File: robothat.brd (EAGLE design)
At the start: 57.6 x 48.2 mm, 84 parts, among them IC3 78L05SMD, T1 BC847, U1 LM293AD, U2 TSM2312CX, U3 ADUM7441ARQZ, U5 TSM2312CX, U8 LM293AD

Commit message: finished first place
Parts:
- removed C3: 100n, rcl:C0805
- moved C11 128.8 mm to (35.1, 18.3), flipped to the bottom, turned to 270 degrees
- moved C7 109.7 mm to (25.4, 17.0), flipped to the bottom, turned to 180 degrees
- moved R11 106.2 mm to (30.5, 13.7), flipped to the bottom, turned to 270 degrees
- moved R9 101.0 mm to (32.8, 18.3), flipped to the bottom, turned to 90 degrees
- moved R12 90.5 mm to (29.5, 17.0), flipped to the bottom, turned to 180 degrees
- moved R15 89.5 mm to (18.0, 7.62), flipped to the bottom, turned to 90 degrees
- moved R14 89.1 mm to (19.1, 2.29), flipped to the bottom, turned to 90 degrees
- moved R4 87.4 mm to (11.7, 13.7), flipped to the bottom, turned to 270 degrees
- moved C1 86.5 mm to (9.14, 4.83), flipped to the bottom, turned to 90 degrees
- moved R1 86.4 mm to (7.11, 4.83), flipped to the bottom, turned to 90 degrees
- moved R3 85.7 mm to (13.7, 13.7), flipped to the bottom, turned to 270 degrees
- moved R2 85.6 mm to (8.13, 8.13), flipped to the bottom
- moved R10 84.6 mm to (32.8, 22.4), flipped to the bottom, turned to 90 degrees
- moved C2 84.2 mm to (9.65, 13.7), flipped to the bottom, turned to 270 degrees
- moved R13 79.2 mm to (27.7, 13.7), flipped to the bottom, turned to 90 degrees
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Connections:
- net AGND: no longer C3.1
- net AX12_RX: now also AXFUSE1.2
- net AX12_RX_P: no longer AXFUSE1.2
- net VCC: no longer C3.2
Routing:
- net BUTTON3: track 0.00 -> 12.7 mm
- net BUTTON1: track 0.00 -> 12.7 mm
- net SENSOR1: track 0.00 -> 11.4 mm, vias 0 -> 1
- net START: track 0.00 -> 10.7 mm
- net BUTTON2: track 0.00 -> 10.7 mm
- net N$18: track 0.00 -> 9.73 mm
- net N$31: track 0.00 -> 8.51 mm
- net LED3: track 0.00 -> 6.11 mm
- net LED1: track 0.00 -> 5.67 mm
- net N$33: track 0.00 -> 3.75 mm
- net N$12: track 0.00 -> 3.66 mm
- net N$41: track 0.00 -> 3.18 mm
- net N$40: track 0.00 -> 3.18 mm
- net N$39: track 0.00 -> 3.18 mm
- net SENSOR2: track 0.00 -> 3.13 mm, vias 0 -> 1
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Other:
- board size 57.6 x 48.2 mm -> 57.6 x 47.9 mm

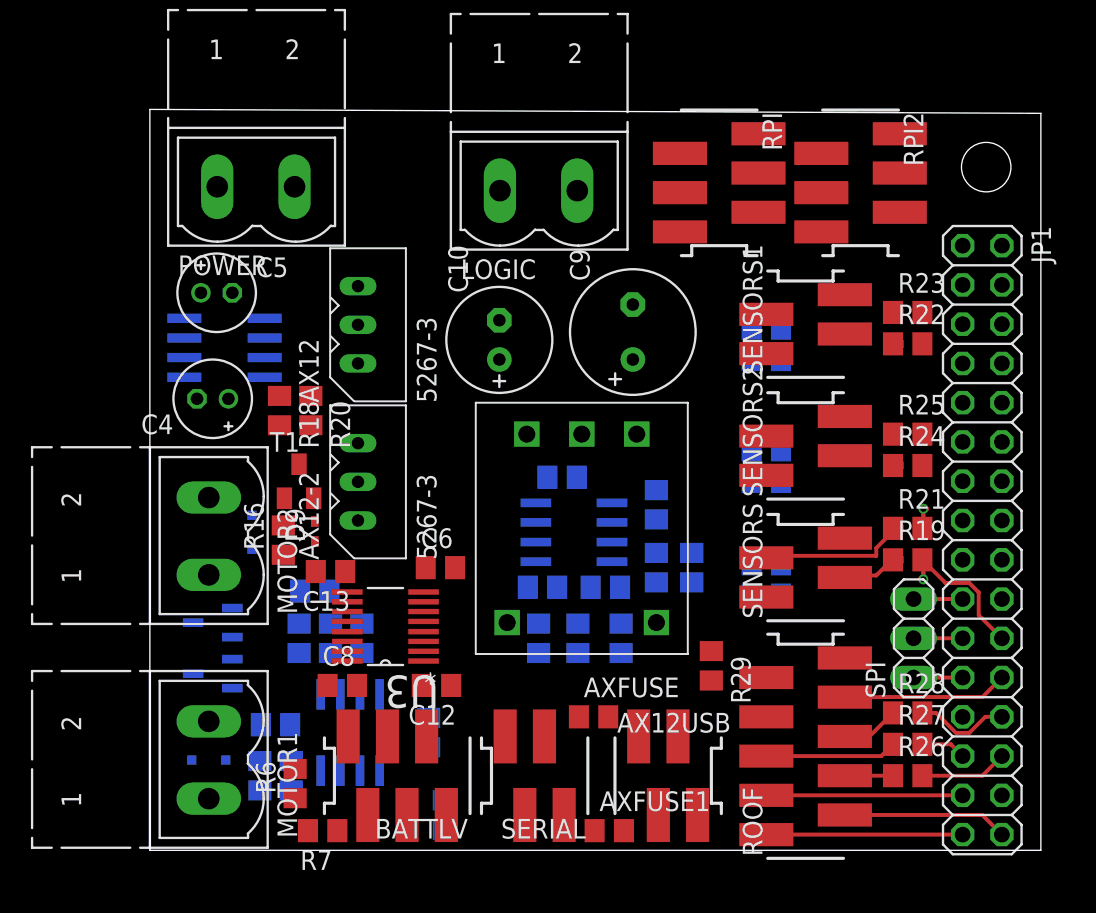
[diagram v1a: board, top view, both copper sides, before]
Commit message: routing and silkscreen done
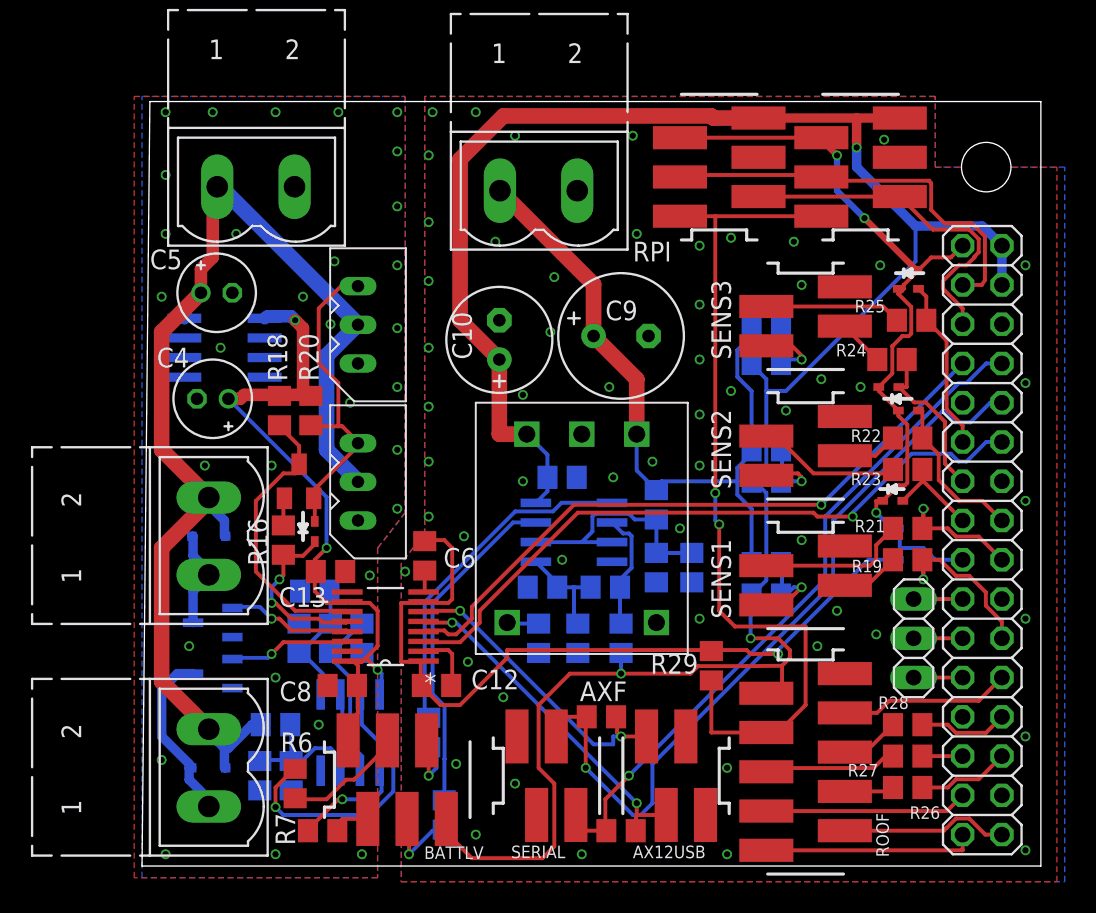
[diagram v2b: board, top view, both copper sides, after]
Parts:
- removed AXFUSE: 0R, resistor:R0805
- removed SENSORS, SENSORS1: (no value), con-amp:SMDTOP4
- added AXF: 0R, resistor:R0805
- added SENS1, SENS3: (no value), con-amp:SMDTOP4
- moved D3 12.2 mm to (48.0, 22.6), flipped to the top, turned to 0 degrees
- moved R23 10.2 mm to (49.0, 24.6)
- moved D5 9.40 mm to (49.0, 36.3), flipped to the top, turned to 0 degrees
- moved R25 7.37 mm to (49.3, 34.3)
- moved R24 6.93 mm to (48.0, 31.8)
- moved R22 6.10 mm to (49.0, 26.7)
- moved D6 5.24 mm to (47.8, 30.0), flipped to the top, turned to 0 degrees
- moved D4 4.32 mm to (49.0, 28.4), flipped to the top, turned to 0 degrees
- moved D8 2.81 mm to (3.81, 20.3), turned to 0 degrees
- moved C6 1.27 mm to (17.8, 19.1), turned to 90 degrees
- moved ROOF 1.02 mm to (42.4, 5.71)
- moved RPI 1.02 mm to (36.8, 44.2)
- moved RPI2 1.02 mm to (46.0, 44.2)
- moved C9 0.80 mm to (30.5, 33.3), turned to 0 degrees
- moved AXFUSE1 0.76 mm to (30.5, 1.27)
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- renumbered SENSORS2 to SENS2
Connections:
- net AX12_TX: now also AXF.2; no longer AXFUSE.2
- net GND: now also SENS1.4, SENS3.4; no longer SENSORS.4, SENSORS1.4
- net N$10: now also SENS2.1; no longer SENSORS1.1
- net N$11: now also SENS2.2; no longer SENSORS1.2
- net N$12: now also SENS1.2; no longer SENSORS.2
- net N$18: now also SENS1.3; no longer SENSORS.3
- net N$22: now also SENS2.3; no longer SENSORS1.3
- net N$26: now also SENS3.1; no longer SENS2.1
- net N$27: now also SENS3.2; no longer SENS2.2
- net N$28: now also SENS3.3; no longer SENS2.3
- net N$9: now also SENS1.1; no longer SENSORS.1
- net RPI_RX: now also AXF.1; no longer AXFUSE.1
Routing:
- net +5V: track 0.00 -> 151.8 mm, vias 0 -> 3
- net +3V3: track 0.00 -> 104.4 mm, vias 0 -> 4
- net VDD: track 0.00 -> 76.1 mm
- net N_RESET: track 0.00 -> 56.1 mm, vias 0 -> 2
- net RPI_RX: track 0.00 -> 50.3 mm, vias 0 -> 1
- net VCC: track 0.00 -> 49.5 mm, vias 0 -> 3
- net +12V: track 0.00 -> 45.9 mm
- net RPI_TX: track 0.00 -> 44.5 mm, vias 0 -> 1
- net MOTOR1: track 0.00 -> 44.0 mm, vias 0 -> 1
- net MOTOR2: track 0.00 -> 42.7 mm, vias 0 -> 1
- net I2C_SDA: track 0.00 -> 27.1 mm
- net I2C_SCL: track 0.00 -> 23.1 mm
- net N$14: track 0.00 -> 22.4 mm
- net AX12_RX: track 0.00 -> 22.4 mm, vias 0 -> 2
- net N$16: track 0.00 -> 21.9 mm
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- added copper zone on layer 1, net AGND
- added copper zone on layer 16, net AGND
- added copper zone on layer 1, net GND
- added copper zone on layer 16, net GND
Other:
- board size 57.6 x 47.9 mm -> 58.1 x 49.5 mm

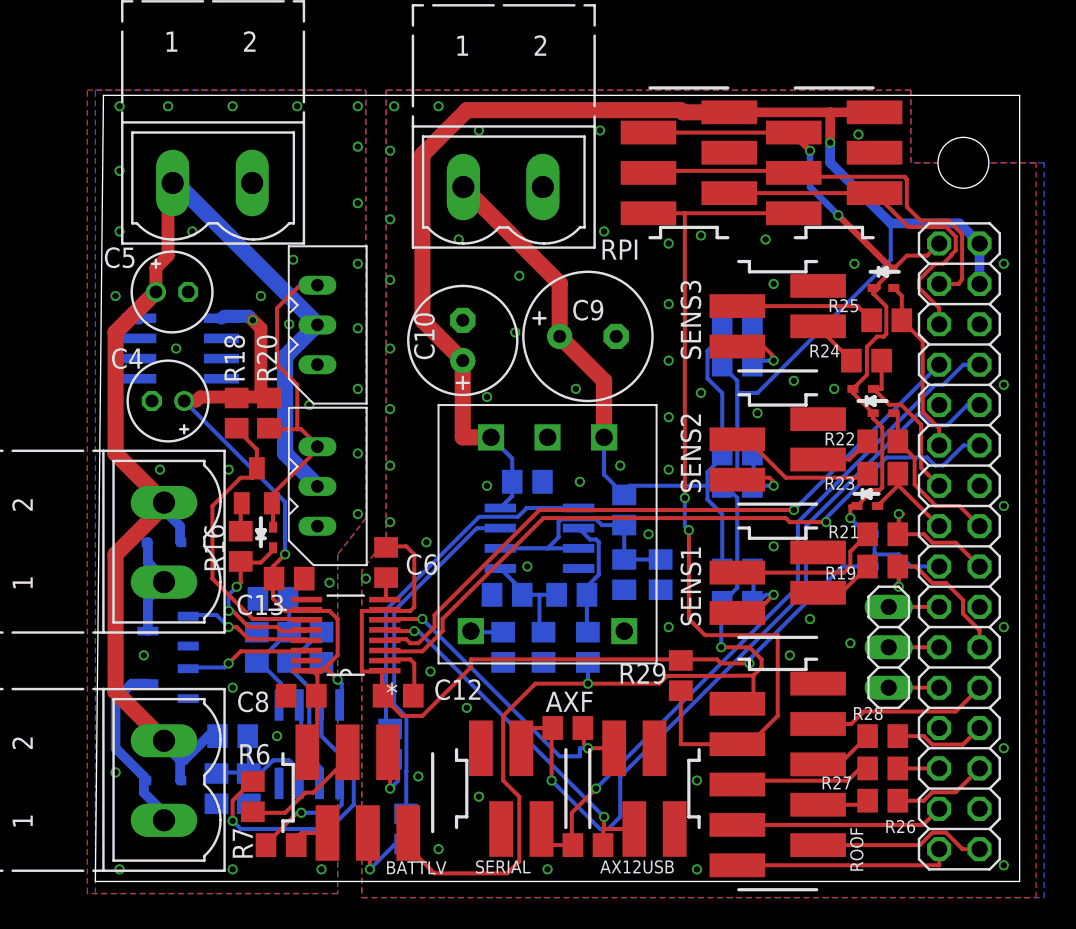
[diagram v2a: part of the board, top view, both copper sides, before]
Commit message: added schematic and pcb in pdf, added BOM
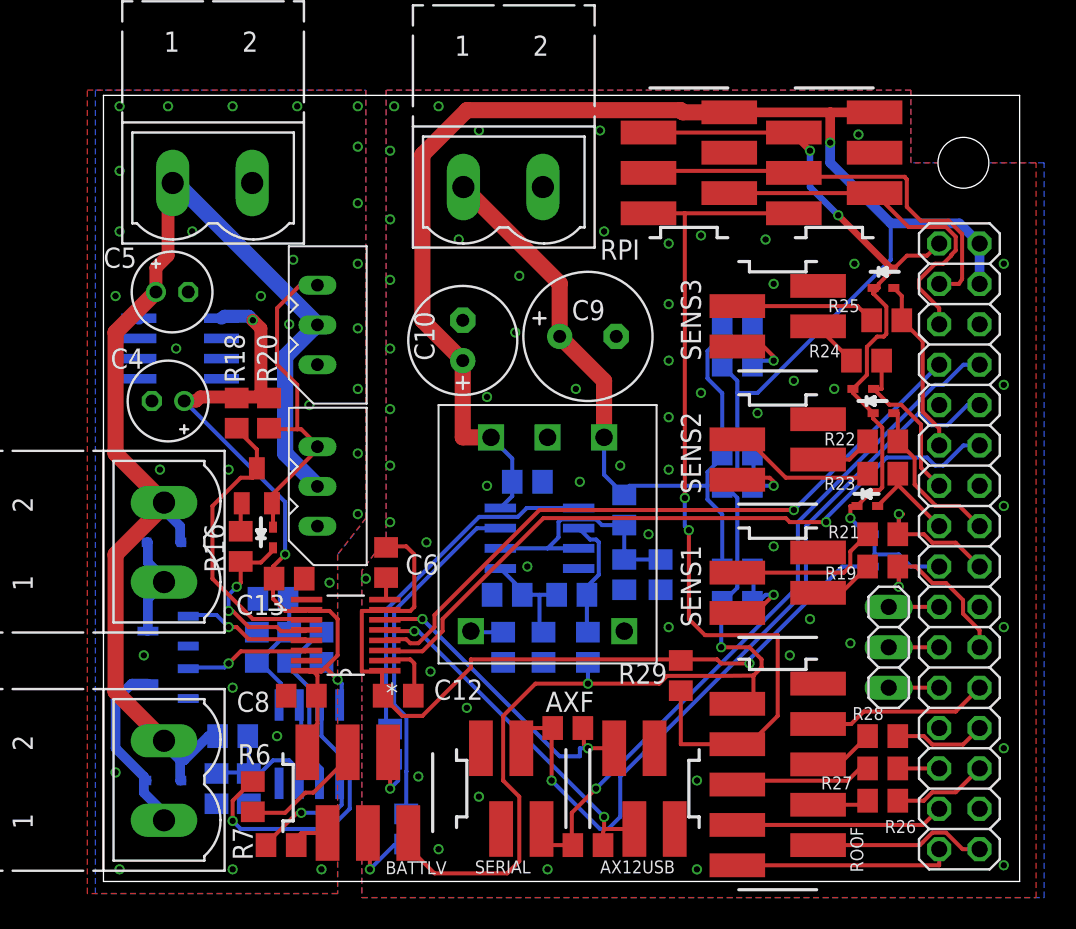
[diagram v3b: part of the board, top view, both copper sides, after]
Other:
- board size 58.1 x 49.5 mm -> 57.6 x 49.5 mm
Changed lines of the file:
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@@
 <board>
 <plain>
-<wire x1="-0.508" y1="-1.016" x2="57.638" y2="-1.016" width="0" layer="20"/>
+<wire x1="0" y1="-1.016" x2="57.638" y2="-1.016" width="0" layer="20"/>
 <wire x1="57.638" y1="-1.016" x2="57.638" y2="48.438" width="0" layer="20"/>
 <wire x1="57.638" y1="48.438" x2="0" y2="48.438" width="0" layer="20"/>
-<wire x1="0" y1="48.438" x2="-0.508" y2="-1.016" width="0" layer="20"/>
+<wire x1="0" y1="48.438" x2="0" y2="-1.016" width="0" layer="20"/>
 <hole x="54.102" y="44.196" drill="3.2"/>
 <circle x="54.102" y="44.196" radius="2.0945375" width="2.54" layer="41"/>
@@
 <wire x1="8.636" y1="2.286" x2="8.128" y2="2.794" width="0.254" layer="16"/>
 <wire x1="14.224" y1="2.286" x2="8.636" y2="2.286" width="0.254" layer="16"/>
-<wire x1="15.748" y1="3.81" x2="14.224" y2="2.286" width="0.254" layer="16"/>
-<wire x1="15.748" y1="6.096" x2="15.748" y2="3.81" width="0.254" layer="16"/>
-<wire x1="13.716" y1="8.128" x2="15.748" y2="6.096" width="0.254" layer="16"/>
+<wire x1="15.494" y1="3.556" x2="14.224" y2="2.286" width="0.254" layer="16"/>
+<wire x1="15.494" y1="6.35" x2="15.494" y2="3.556" width="0.254" layer="16"/>
+<wire x1="13.716" y1="8.128" x2="15.494" y2="6.35" width="0.254" layer="16"/>
 <wire x1="13.716" y1="9.906" x2="13.716" y2="8.128" width="0.254" layer="16"/>
 <wire x1="9.398" y1="5.08" x2="9.398" y2="5.268" width="0.254" layer="1"/>
